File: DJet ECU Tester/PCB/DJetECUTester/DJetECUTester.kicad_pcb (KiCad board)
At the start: 2 copper layers, 93 x 79 mm, 103 parts, among them J1 ISP, J10 ECU3, J2 ECU1, J3 USB_B_Mini, J4 BREAKOUT, J5 12V IN, J6 MPS, J7 VAC, J8 INJECTORS, J9 ECU2, Q1 MMBT2222ALT1G, Q10 MMBT2222ALT1G, Q11 MMBT2222ALT1G, Q12 MMBT3906LT1G, Q13 MMBT3906LT1G, Q14 MMBT3906LT1G, Q2 MMBT2222ALT1G, Q3 MMBT2222ALT1G, Q4 MMBT2222ALT1G, Q5 MMBT2222ALT1G, Q6 MMBT2222ALT1G, Q7 MMBT2222ALT1G, Q8 MMBT2222ALT1G, Q9 MMBT2222ALT1G, U1 ATmega328P, U2 LM2596S-5, U3 FT232RL, U4 MCP41HV51-502E-ST, U5 MCP41HV51-502E-ST, Y1 FA-238 16.0000MB-C3

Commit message: Work in progress.
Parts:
- removed J7: VAC, TerminalBlock_TE-Connectivity:TerminalBlock_TE_282834-6_1x06_P2.54mm_Horizontal
- removed J8: INJECTORS, Britishideas:PhoenixContact_COMBICON_PT_5
- removed JP4: VAC VCC, Connector_PinHeader_2.54mm:PinHeader_1x03_P2.54mm_Vertical
- removed Q13, Q14: MMBT3906LT1G, Package_TO_SOT_SMD:SOT-23
- added C18: 100nF, Capacitor_SMD:C_0805_2012Metric, F.Cu at (299.5, 127.2)
- added C19: 100nF, Capacitor_SMD:C_0805_2012Metric, F.Cu at (464.8, 14.4)
- added C20: 100nF, Capacitor_SMD:C_0805_2012Metric, F.Cu at (463.2, 21.0)
- added D10: MBR0520LT1G, Britishideas:SOD-123, F.Cu at (305.0, 116.4)
- added D5: MBR0520LT1G, Britishideas:SOD-123, F.Cu at (352.3, 92.6)
- added D6: MBR0520LT1G, Britishideas:SOD-123, F.Cu at (357.5, 92.6)
- added D7: MBR0520LT1G, Britishideas:SOD-123, F.Cu at (341.8, 92.6)
- added D8: RED, LED_SMD:LED_PLCC-2, F.Cu at (294.2, 128.1)
- added D9: MBR0520LT1G, Britishideas:SOD-123, F.Cu at (305.0, 113.9)
- added JP1: COOLANTTEMP, Connector_PinHeader_2.54mm:PinHeader_2x01_P2.54mm_Vertical, F.Cu at (456.1, 21.8)
- added L2: 1.5mH, Britishideas:D-Jetronic-Injector-Inductor-Multi-Component, F.Cu at (404.4, 71.8)
- added L3: 1.5mH, Britishideas:D-Jetronic-Injector-Inductor-Multi-Component, F.Cu at (404.4, 32.5)
- added L4: 1.5mH, Britishideas:D-Jetronic-Injector-Inductor-Multi-Component, F.Cu at (365.2, 71.8)
- added L5: 1.5mH, Britishideas:D-Jetronic-Injector-Inductor-Multi-Component, F.Cu at (365.2, 32.5)
- added L6: 1.5mH, Britishideas:D-Jetronic-Injector-Inductor-Multi-Component, F.Cu at (286.7, 32.5)
- added L7: 1.5mH, Britishideas:D-Jetronic-Injector-Inductor-Multi-Component, F.Cu at (326.0, 71.8)
- added L8: 1.5mH, Britishideas:D-Jetronic-Injector-Inductor-Multi-Component, F.Cu at (326.0, 32.5)
- added L9: 1.5mH, Britishideas:D-Jetronic-Injector-Inductor-Multi-Component, F.Cu at (286.7, 71.8)
- added R39: 11k, Resistor_SMD:R_0805_2012Metric, F.Cu at (368.3, 92.8)
- added R40: 10k, Resistor_SMD:R_0805_2012Metric, F.Cu at (343.0, 99.9)
- added R41: 11k, Resistor_SMD:R_0805_2012Metric, F.Cu at (446.7, 14.4)
- added R42: 10k, Resistor_SMD:R_0805_2012Metric, F.Cu at (442.3, 17.4)
- added R43: 11k, Resistor_SMD:R_0805_2012Metric, F.Cu at (351.9, 105.8)
- added R44: 1K, Resistor_SMD:R_0805_2012Metric, F.Cu at (308.3, 128.0)
- added R45: 100k, Resistor_SMD:R_0805_2012Metric, F.Cu at (469.2, 14.4)
- added R46: 2.7, Britishideas:Chip Resistor 5329 13573 Metric, F.Cu at (312.1, 104.0)
- added R47: 2.7, Britishideas:Chip Resistor 5329 13573 Metric, F.Cu at (327.6, 95.6)
- added R48: 4k2, Resistor_SMD:R_0805_2012Metric, F.Cu at (308.3, 125.1)
- added R49: 4k2, Resistor_SMD:R_0805_2012Metric, F.Cu at (303.9, 127.2)
- added R50: 2.7, Britishideas:Chip Resistor 5329 13573 Metric, F.Cu at (312.1, 95.6)
- added R51: 2.7, Britishideas:Chip Resistor 5329 13573 Metric, F.Cu at (327.6, 104.0)
- added R52: 10k, Resistor_SMD:R_0805_2012Metric, F.Cu at (306.2, 122.1)
- added R53: 10k, Resistor_SMD:R_0805_2012Metric, F.Cu at (306.2, 119.2)
- added R54: 2.7, Britishideas:Chip Resistor 5329 13573 Metric, F.Cu at (296.6, 104.0)
- added R55: 2.7, Britishideas:Chip Resistor 5329 13573 Metric, F.Cu at (281.1, 104.0)
- added R58: 2.7, Britishideas:Chip Resistor 5329 13573 Metric, F.Cu at (296.6, 95.6)
- added R59: 2.7, Britishideas:Chip Resistor 5329 13573 Metric, F.Cu at (281.1, 95.6)
- added TP10: TestPoint, TestPoint:TestPoint_Pad_D2.0mm, F.Cu at (467.4, 22.0)
- added TP11: TestPoint, TestPoint:TestPoint_Pad_D2.0mm, F.Cu at (469.0, 17.9)
- added U6: MCP23S08T-E_SO, Package_SO:SOIC-18W_7.5x11.6mm_P1.27mm, F.Cu at (297.5, 119.2)
- added U7: MCP41HV51-502E-ST, Package_SO:TSSOP-14_4.4x5mm_P0.65mm, F.Cu at (458.1, 16.2)
- D1: value RED -> MBR0520LT1G; footprint LED_SMD:LED_PLCC-2 -> Britishideas:SOD-123
- J4: value BREAKOUT -> 12V 4A IN (5.5/2.5); footprint Connector_PinHeader_2.54mm:PinHeader_2x13_P2.54mm_Vertical -> Connector_BarrelJack:BarrelJack_Wuerth_6941xx301002
- Q12: value MMBT3906LT1G -> MMBT2222ALT1G
- R25, R26, R32, R33, R38: value 1k -> 10k
- R28, R29, R30: value 10k -> 100k
- R31: value 1k -> 100k
- R37: value 10k -> 11k
- R5: value 1K -> 10k
- moved R36 273.3 mm to (437.9, 14.4), turned to 0 degrees
- moved R25 260.8 mm to (437.9, 20.3)
- moved R34 240.5 mm to (442.3, 14.4), turned to 0 degrees
- moved R38 228.1 mm to (437.9, 17.4), turned to 0 degrees
- moved R31 165.3 mm to (351.9, 99.9), turned to 0 degrees
- moved R28 163.6 mm to (356.3, 102.9), turned to 0 degrees
- moved R5 160.7 mm to (360.7, 99.9), turned to 0 degrees
- moved R26 160.3 mm to (356.3, 99.9)
- moved R27 159.4 mm to (351.9, 102.9), turned to 0 degrees
- moved R29 158.0 mm to (347.4, 105.8), turned to 0 degrees
- moved Q10 153.2 mm to (347.5, 96.2), turned to 0 degrees
- moved R37 152.3 mm to (343.0, 105.8), turned to 0 degrees
- moved Q9 152.2 mm to (343.1, 96.2), turned to 0 degrees
- moved R30 150.8 mm to (347.4, 99.9), turned to 0 degrees
- moved R32 149.9 mm to (343.0, 102.9)
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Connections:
- net /~COOLANTTEMP_CS renamed /~COOLANTTEMP1_CS
- D1 pad 2: +5V -> Net-(D1-Pad2)
- J10 pad 7: /ECU_DIAGGROUP13-25 -> (no net)
- J4 pad 1: /ECU_AIRTEMP-1 -> +12V
- J4 pad 2: /ECU_TPSWOT-2 -> GND
- J4 pad 3: /ECU_INJGROUP1-3 -> GND
- Q10 pad 1: Net-(Q10-Pad1) -> Net-(D5-Pad1)
- Q10 pad 3: Net-(J7-Pad4) -> Net-(Q10-Pad3)
- Q11 pad 1: Net-(Q11-Pad1) -> Net-(D6-Pad1)
- Q12 pad 1: Net-(Q12-Pad1) -> Net-(D7-Pad1)
- Q12 pad 2: +12V -> GND
- Q12 pad 3: /ECU_START-18 -> Net-(Q12-Pad3)
- Q9 pad 1: Net-(Q9-Pad1) -> Net-(D1-Pad1)
- Q9 pad 3: Net-(J7-Pad2) -> Net-(Q9-Pad3)
- R25 pad 1: Net-(Q9-Pad1) -> Net-(D5-Pad2)
- R25 pad 2: /VAC1 -> /ECU_INJGROUP2-4
- R26 pad 1: Net-(Q10-Pad1) -> Net-(D6-Pad2)
- R26 pad 2: /VAC2 -> /ECU_INJGROUP4-6
- R27 pad 1: Net-(Q9-Pad1) -> Net-(D7-Pad2)
- R27 pad 2: GND -> /ECU_INJGROUP3-5
- R28 pad 1: Net-(Q10-Pad1) -> Net-(D1-Pad1)
- R29 pad 1: /Vacuum/VACVCC -> Net-(D5-Pad1)
- R29 pad 2: Net-(J7-Pad2) -> GND
- R30 pad 1: /Vacuum/VACVCC -> Net-(D6-Pad1)
- R30 pad 2: Net-(J7-Pad4) -> GND
- R31 pad 1: Net-(Q13-Pad1) -> Net-(D7-Pad1)
- R31 pad 2: Net-(J7-Pad2) -> GND
- R32 pad 1: Net-(Q14-Pad1) -> +12V
- R32 pad 2: Net-(J7-Pad4) -> Net-(Q9-Pad3)
- R33 pad 1: Net-(Q11-Pad1) -> +12V
- R33 pad 2: /START -> Net-(Q10-Pad3)
- R34 pad 1: Net-(Q11-Pad1) -> +12V
- R34 pad 2: GND -> Net-(Q11-Pad3)
- R35 pad 2: Net-(Q11-Pad3) -> Net-(Q12-Pad3)
- R36 pad 1: Net-(J7-Pad3) -> Net-(Q9-Pad3)
- R36 pad 2: GND -> /MCU_INJGROUP1-3
- R37 pad 1: Net-(J7-Pad5) -> /MCU_INJGROUP1-3
- R38 pad 1: Net-(Q12-Pad1) -> Net-(Q10-Pad3)
- R38 pad 2: Net-(Q11-Pad3) -> /MCU_INJGROUP2-4
- R5 pad 1: Net-(D1-Pad1) -> Net-(D1-Pad2)
- R5 pad 2: /STATUS -> /ECU_INJGROUP1-3
- TP4 pad 1: GND -> Net-(JP1-Pad1)
- U1 pad 11: /START -> /MCU_INJGROUP2-4
- U1 pad 12: /TPSWOT -> /~COOLANTTEMP2_CS
- U1 pad 19: Net-(U1-Pad19) -> (no net)
- U1 pad 2: /VAC1 -> /MCU_INJGROUP3-5
- U1 pad 22: Net-(U1-Pad22) -> (no net)
- U1 pad 23: /TPSIDLE -> /MCU_INJGROUP4-6
- U1 pad 24: /TPSACCEL2 -> (no net)
- U1 pad 25: /TPSACCEL1 -> /~IO_CS
- U1 pad 32: /VAC2 -> /MCU_INJGROUP1-3
- U3 pad 10: Net-(U3-Pad10) -> (no net)
- U3 pad 11: Net-(U3-Pad11) -> (no net)
- U3 pad 12: Net-(U3-Pad12) -> (no net)
- U3 pad 13: Net-(U3-Pad13) -> (no net)
- U3 pad 14: Net-(U3-Pad14) -> (no net)
- U3 pad 19: Net-(U3-Pad19) -> (no net)
- U3 pad 22: Net-(U3-Pad22) -> (no net)
- U3 pad 23: Net-(U3-Pad23) -> (no net)
- U3 pad 27: Net-(U3-Pad27) -> (no net)
- U3 pad 28: Net-(U3-Pad28) -> (no net)
- U3 pad 3: Net-(U3-Pad3) -> (no net)
- U3 pad 6: Net-(U3-Pad6) -> (no net)
- U3 pad 9: Net-(U3-Pad9) -> (no net)
- U4 pad 13: Net-(U4-Pad13) -> (no net)
- U4 pad 8: Net-(U4-Pad8) -> (no net)
- U5 pad 11: GND -> Net-(JP1-Pad1)
- U5 pad 13: Net-(U5-Pad13) -> (no net)
- U5 pad 8: Net-(U5-Pad8) -> (no net)
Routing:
- net /MPS-15: track 146.9 -> 0.00 mm, vias 5 -> 0
- net /ECU_TPSIDLE-17: track 111.3 -> 0.00 mm, vias 1 -> 0
- net +12V: track 177.9 -> 70.9 mm, vias 7 -> 2
- net /MPS-7: track 103.5 -> 0.00 mm, vias 2 -> 0
- net /ECU_AIRTEMP-1: track 102.1 -> 0.00 mm, vias 2 -> 0
- net /ECU_TPSACCEL1-9: track 101.0 -> 0.00 mm, vias 1 -> 0
- net /ECU_TPSWOT-2: track 97.1 -> 0.13 mm, vias 2 -> 0
- net /ECU_START-18: track 79.7 -> 0.00 mm, vias 5 -> 0
- net /MPS-10: track 103.0 -> 29.5 mm, vias 3 -> 2
- net /ECU_INJGROUP1-3: track 74.7 -> 9.94 mm, vias 2 -> 0
- net /ECU_TPSACCEL2-20: track 61.4 -> 0.00 mm, vias 2 -> 0
- net /ECU_INJGROUP2-4: track 66.3 -> 10.0 mm, vias 3 -> 1
- net /Vacuum/VACVCC: track 47.5 -> 0.00 mm, vias 2 -> 0
- net /ECU_FUELPUMPRELAY-19: track 46.2 -> 0.00 mm, vias 2 -> 0
- net /START: track 43.6 -> 0.00 mm, vias 2 -> 0
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- removed copper zone on B.Cu, net GND
- removed copper zone on F.Cu, net GND
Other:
- board text added: "(C) ANDY@BRITISHIDEAS.COM 2022"
- board text added: "MERCEDES V8 DJET ECU TESTER V2.0"
- board text removed: "(C) ANDY@BRITISHIDEAS.COM 2021"
- board text removed: "5V"
- board text removed: "BRKOUT"
- board text removed: "G"
- board text removed: "INJ GRP"
- board text removed: "MERCEDES V8 DJET ECU TESTER V1.1"
- board text removed: "VAC"
- board text removed: "VACVCC"
- board text removed: "VCC"
- board text removed: "X"

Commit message: Working on new PCB.
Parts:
- removed R55, R58, R59: 2.7, Britishideas:Chip Resistor 5329 13573 Metric
- added D11: RED, LED_SMD:LED_PLCC-2, F.Cu at (328.1, 73.5)
- added J7: Conn_01x01, Britishideas:tabconnector-63849-1, F.Cu at (317.5, 78.5)
- added J8: Conn_01x01, Britishideas:tabconnector-63849-1, F.Cu at (322.5, 78.5)
- added L10: 680uH, Britishideas:Inductor-MSS1210-684KED, F.Cu at (310.5, 129.5)
- added L11: 680uH, Britishideas:Inductor-MSS1210-684KED, F.Cu at (296.5, 129.5)
- added L12: 680uH, Britishideas:Inductor-MSS1210-684KED, F.Cu at (282.0, 129.5)
- added L13: 680uH, Britishideas:Inductor-MSS1210-684KED, F.Cu at (268.0, 129.5)
- added L14: 680uH, Britishideas:Inductor-MSS1210-684KED, F.Cu at (310.5, 116.0)
- added L15: 680uH, Britishideas:Inductor-MSS1210-684KED, F.Cu at (296.5, 116.0)
- added L16: 680uH, Britishideas:Inductor-MSS1210-684KED, F.Cu at (282.0, 116.0)
- added L17: 680uH, Britishideas:Inductor-MSS1210-684KED, F.Cu at (268.0, 116.0)
- L2, L3, L4, L5, L6, L7, L8, L9: value 1.5mH -> 680uH; footprint Britishideas:D-Jetronic-Injector-Inductor-Multi-Component -> Britishideas:Inductor-MSS1210-684KED
- R46, R47, R50, R51: value 2.7 -> 50; footprint Britishideas:Chip Resistor 5329 13573 Metric -> Britishideas:Potentometer_Bourns_PV36W
- R54: value 2.7 -> 2k6; footprint Britishideas:Chip Resistor 5329 13573 Metric -> Resistor_SMD:R_0805_2012Metric
- moved R45 268.6 mm to (211.4, 89.7)
- moved C19 264.1 mm to (210.8, 87.0), turned to 90 degrees
- moved C20 256.1 mm to (213.8, 79.5)
- moved U7 252.8 mm to (214.8, 84.8), turned to 90 degrees
- moved TP10 251.7 mm to (221.8, 76.6)
- moved TP11 250.5 mm to (225.5, 76.6)
- moved JP1 242.0 mm to (221.8, 82.4), turned to 90 degrees
- moved L3 121.8 mm to (296.5, 89.0), turned to 270 degrees
- moved L5 112.4 mm to (268.0, 89.0), turned to 270 degrees
- moved R44 104.3 mm to (205.7, 109.4), turned to 90 degrees
- moved L2 95.5 mm to (310.5, 89.0), turned to 270 degrees
- moved D8 94.7 mm to (201.4, 109.7), turned to 180 degrees
- moved R25 89.0 mm to (363.9, 69.8)
- moved R34 89.0 mm to (368.3, 63.9)
- moved R36 89.0 mm to (363.9, 63.9)
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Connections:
- J2 pad 1: +12V -> /ECU_PWR
- J2 pad 2: +12V -> /ECU_PWR
- L2 pad 1: Net-(L2-Pad1) -> /ECU_INJGROUP1-3
- L2 pad 2: /ECU_INJGROUP1-3 -> Net-(L2-Pad2)
- L3 pad 1: Net-(L3-Pad1) -> Net-(L2-Pad2)
- L3 pad 2: /ECU_INJGROUP3-5 -> Net-(L3-Pad2)
- L4 pad 1: Net-(L4-Pad1) -> Net-(L3-Pad2)
- L4 pad 2: /ECU_INJGROUP3-5 -> Net-(L4-Pad2)
- L5 pad 1: Net-(L5-Pad1) -> Net-(L4-Pad2)
- L5 pad 2: /ECU_INJGROUP1-3 -> GND
- L6 pad 1: Net-(L6-Pad1) -> /ECU_INJGROUP2-4
- L6 pad 2: /ECU_INJGROUP4-6 -> Net-(L6-Pad2)
- L7 pad 1: Net-(L7-Pad1) -> Net-(L6-Pad2)
- L7 pad 2: /ECU_INJGROUP2-4 -> Net-(L7-Pad2)
- L8 pad 1: Net-(L8-Pad1) -> Net-(L7-Pad2)
- L8 pad 2: /ECU_INJGROUP4-6 -> Net-(L8-Pad2)
- L9 pad 1: Net-(L9-Pad1) -> Net-(L8-Pad2)
- L9 pad 2: /ECU_INJGROUP2-4 -> GND
- R46 pad 1: Net-(L2-Pad1) -> /ECU_INJGROUP1-3
- R47 pad 1: Net-(L3-Pad1) -> /ECU_INJGROUP2-4
- R50 pad 1: Net-(L4-Pad1) -> /ECU_INJGROUP4-6
- R51 pad 1: Net-(L5-Pad1) -> /ECU_INJGROUP3-5
- R54 pad 1: Net-(L6-Pad1) -> Net-(D11-Pad1)
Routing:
- net +12V: track 70.9 -> 201.4 mm
- net /ECU_INJGROUP1-3: track 9.94 -> 125.1 mm, vias 0 -> 2
- net /ECU_INJGROUP2-4: track 10.0 -> 107.7 mm, vias 1 -> 2
- net /ECU_TPSIDLE-17: track 0.00 -> 91.2 mm, vias 0 -> 3
- net /ECU_INJGROUP3-5: track 11.9 -> 98.3 mm, vias 1 -> 2
- net /ECU_INJGROUP4-6: track 11.9 -> 92.9 mm, vias 1 -> 0
- net /MPS-8: track 79.8 -> 0.00 mm, vias 1 -> 0
- net /ECU_TPSACCEL1-9: track 0.00 -> 73.8 mm, vias 0 -> 3
- net /ECU_TPSACCEL2-20: track 0.00 -> 73.6 mm, vias 0 -> 3
- net /ECU_TPSWOT-2: track 0.13 -> 63.2 mm, vias 0 -> 1
- net /ECU_COOLANTTEMP-23: track 0.00 -> 52.0 mm, vias 0 -> 3
- net /ECU_TRIGGERGROUP1-21: track 0.00 -> 50.5 mm, vias 0 -> 5
- net /ECU_AIRTEMP-1: track 0.00 -> 49.4 mm, vias 0 -> 1
- net /MPS-10: track 29.5 -> 1.27 mm, vias 2 -> 0
- net Net-(JP1-Pad1): track 0.00 -> 25.8 mm, vias 0 -> 3
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- added copper zone on B.Cu, net GND
- added copper zone on F.Cu, net GND
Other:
- board size 93 x 79 mm -> 162 x 90 mm
- board text added: "ECU PWR"

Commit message: Working on new PCB.
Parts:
- moved R35 167.9 mm to (245.2, 132.4), turned to 180 degrees
- moved R39 164.3 mm to (245.2, 117.6)
- moved D6 162.4 mm to (250.6, 139.4)
- moved Q11 158.1 mm to (247.2, 138.6), turned to 180 degrees
- moved Q12 156.6 mm to (247.2, 129.6), turned to 180 degrees
- moved R26 154.3 mm to (252.8, 137.6)
- moved R40 151.1 mm to (244.4, 138.8), turned to 90 degrees
- moved R30 148.9 mm to (250.0, 136.8), turned to 90 degrees
- moved R43 148.1 mm to (245.2, 127.0)
- moved D5 147.7 mm to (250.4, 121.0)
- moved R31 147.6 mm to (249.8, 127.7), turned to 90 degrees
- moved R41 146.4 mm to (245.2, 135.8)
- moved R34 145.5 mm to (245.2, 141.4), turned to 180 degrees
- moved D7 144.8 mm to (250.2, 130.4)
- moved R27 144.1 mm to (252.6, 128.6)
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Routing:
- net /MPS-7: track 0.00 -> 63.3 mm
- net /MPS-8: track 0.00 -> 52.6 mm
- net /MPS-10: track 1.27 -> 38.2 mm
- net /ECU_TRIGGERGROUP2-13: track 63.7 -> 40.2 mm
- net /ECU_TRIGGERGROUP3-22: track 47.1 -> 70.3 mm
- net /ECU_TRIGGERGROUP1-21: track 50.5 -> 73.1 mm
- net /ECU_TRIGGERGROUP4-14: track 65.0 -> 42.5 mm
- net /ECU_TPSACCEL2-20: track 73.6 -> 95.4 mm
- net /ECU_COOLANTTEMP-23: track 52.0 -> 73.7 mm
- net /ECU_TPSIDLE-17: track 91.2 -> 70.7 mm
- net /ECU_AIRTEMP-1: track 49.4 -> 67.7 mm, vias 1 -> 3
- net /MPS-15: track 0.00 -> 17.4 mm
- net /ECU_TPSACCEL1-9: track 73.8 -> 56.8 mm, vias 3 -> 1
- net /ECU_TPSWOT-2: track 63.2 -> 75.4 mm, vias 1 -> 3
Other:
- board text added: "ECU I/O"
- board text added: "PWR+INJ"
- board text removed: "(10)"
- board text removed: "(15)"
- board text removed: "(7)"
- board text removed: "(8)"
- board text removed: "bl"
- board text removed: "gn"
- board text removed: "grey +"
- board text removed: "rt"
- board text removed: "sw"

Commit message: Initial routing completed.
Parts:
- moved Q12 0.20 mm to (247.2, 129.8)
- moved R27 0.20 mm to (252.8, 128.6)
- moved R33 0.20 mm to (245.2, 123.2)
- moved R31 0.20 mm to (250.0, 127.7)
- moved R34 0.20 mm to (245.2, 141.6)
- moved R35 0.20 mm to (245.2, 132.6)
- moved R39 0.20 mm to (245.2, 117.4)
- moved R25 0.11 mm to (252.8, 119.2)
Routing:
- net +12V: track 201.4 -> 275.8 mm, vias 2 -> 7
- net /ECU_START-18: track 0.00 -> 65.5 mm, vias 0 -> 3
- net /MCU_INJGROUP1-3: track 0.00 -> 63.4 mm, vias 0 -> 4
- net /ECU_FUELPUMPRELAY-19: track 0.00 -> 62.5 mm, vias 0 -> 3
- net /MISO: track 41.9 -> 103.7 mm, vias 5 -> 11
- net /MOSI: track 42.3 -> 103.9 mm, vias 6 -> 10
- net /SCK: track 45.4 -> 106.3 mm, vias 6 -> 10
- net /~IO_CS: track 0.00 -> 60.8 mm, vias 0 -> 6
- net /MCU_INJGROUP4-6: track 0.00 -> 60.2 mm, vias 0 -> 2
- net +5V: track 176.5 -> 226.2 mm, vias 10 -> 14
- net /MCU_INJGROUP3-5: track 0.00 -> 45.7 mm, vias 0 -> 2
- net /TPSACCEL1: track 22.4 -> 66.5 mm, vias 2 -> 6
- net /TPSWOT: track 14.8 -> 53.0 mm, vias 0 -> 6
- net /MCU_INJGROUP2-4: track 0.00 -> 36.4 mm, vias 0 -> 2
- net /~COOLANTTEMP2_CS: track 4.06 -> 38.3 mm, vias 0 -> 2
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
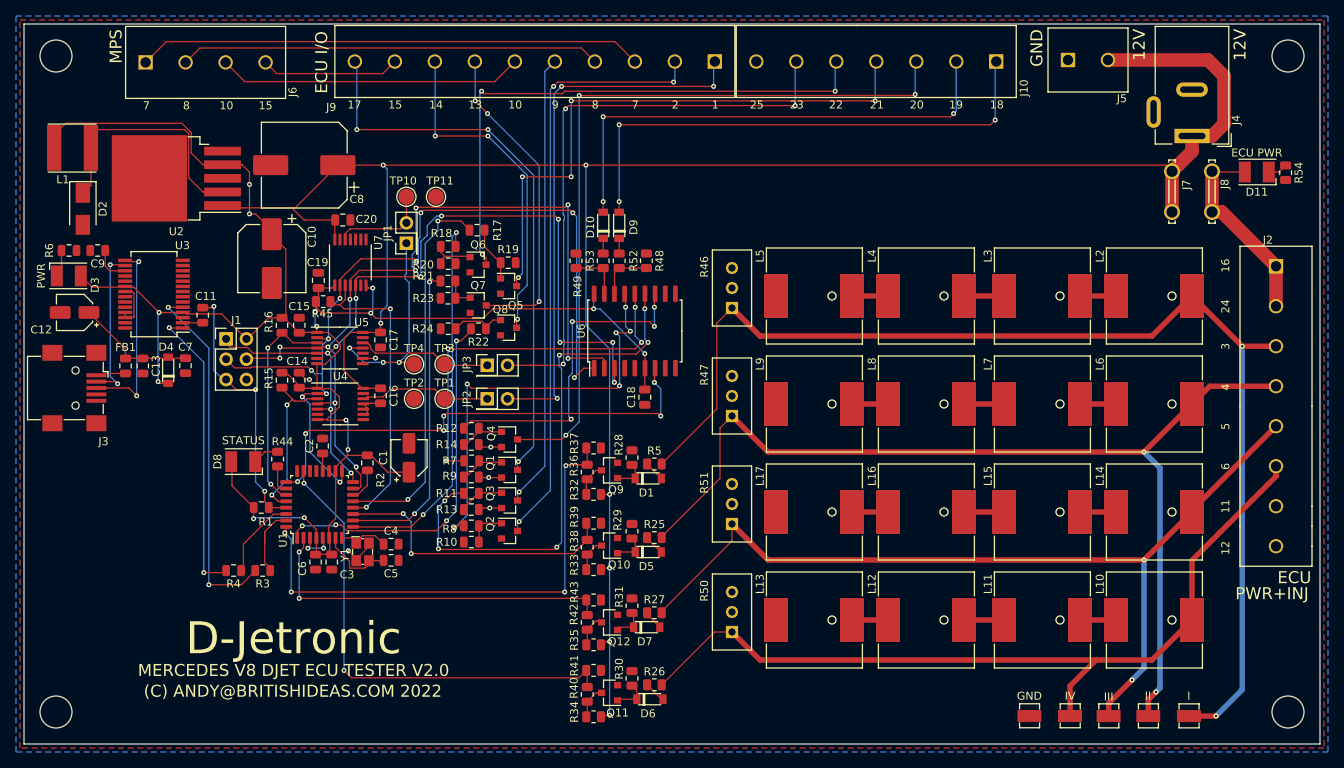
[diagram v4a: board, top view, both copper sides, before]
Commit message: Tweaked PCB layout, added basic ground stitching vias. Regenerated BOM.
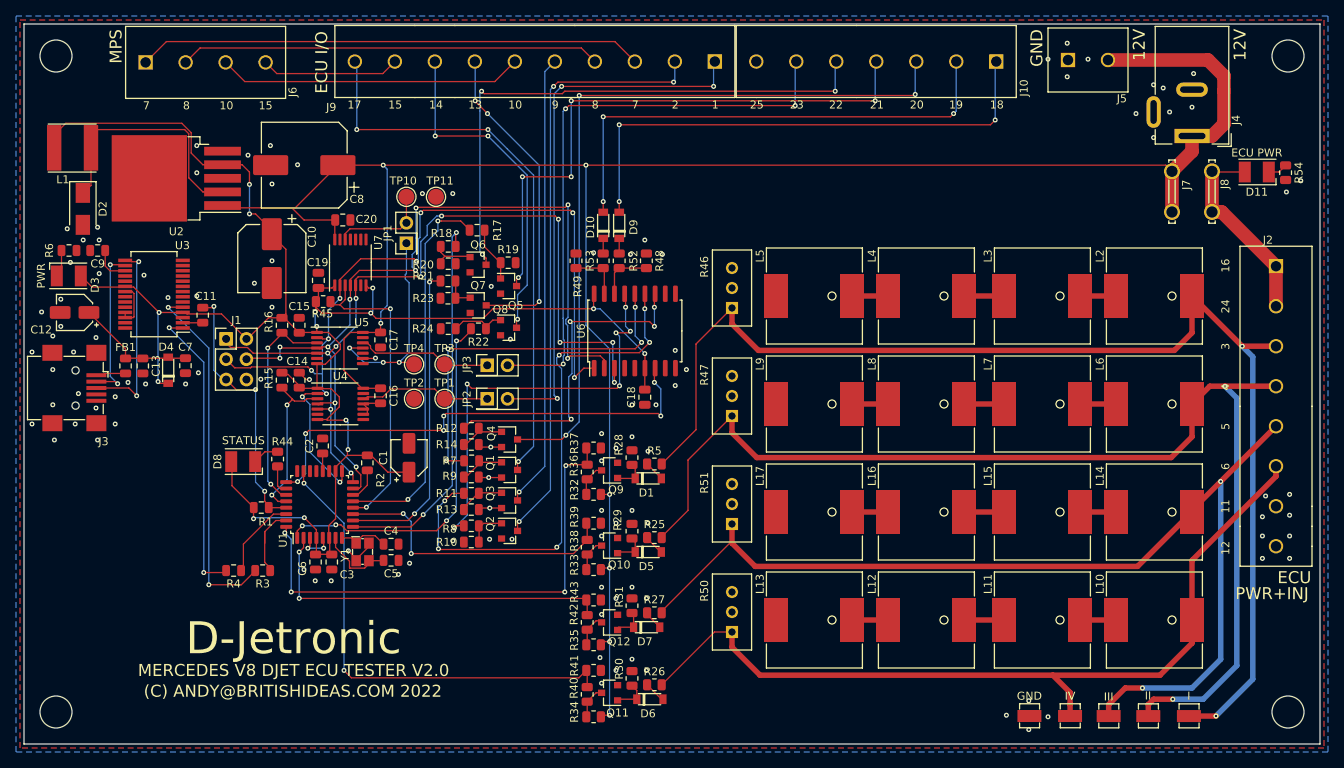
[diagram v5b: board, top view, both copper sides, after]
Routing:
- net /ECU_INJGROUP3-5: track 113.1 -> 133.8 mm
- net /ECU_INJGROUP2-4: track 126.6 -> 146.4 mm
- net /ECU_INJGROUP1-3: track 148.3 -> 154.7 mm
- net /ECU_INJGROUP4-6: track 104.5 -> 106.6 mm
- net /TPSACCEL1: track 66.5 -> 67.0 mm
- net GND: vias 8 -> 114

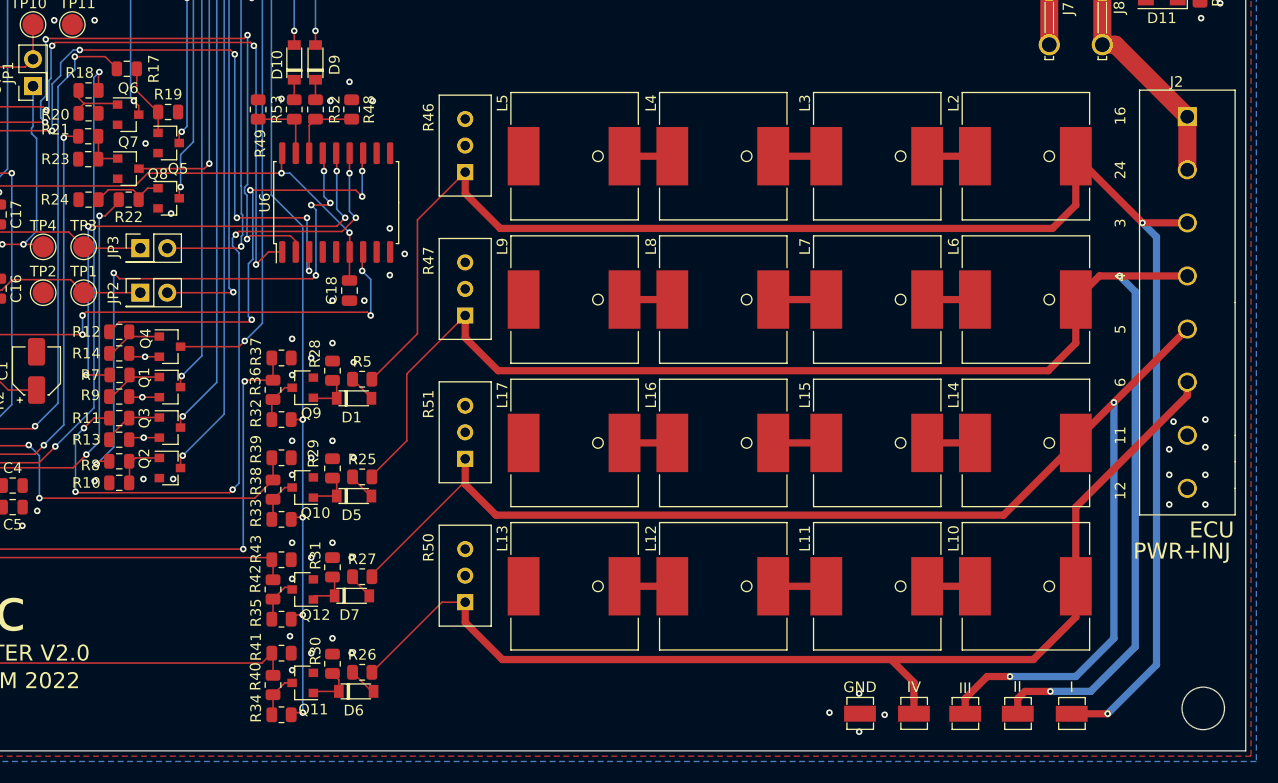
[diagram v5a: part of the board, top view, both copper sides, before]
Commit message: Added test points from trimpots. Added ground stitching vias around inductors.
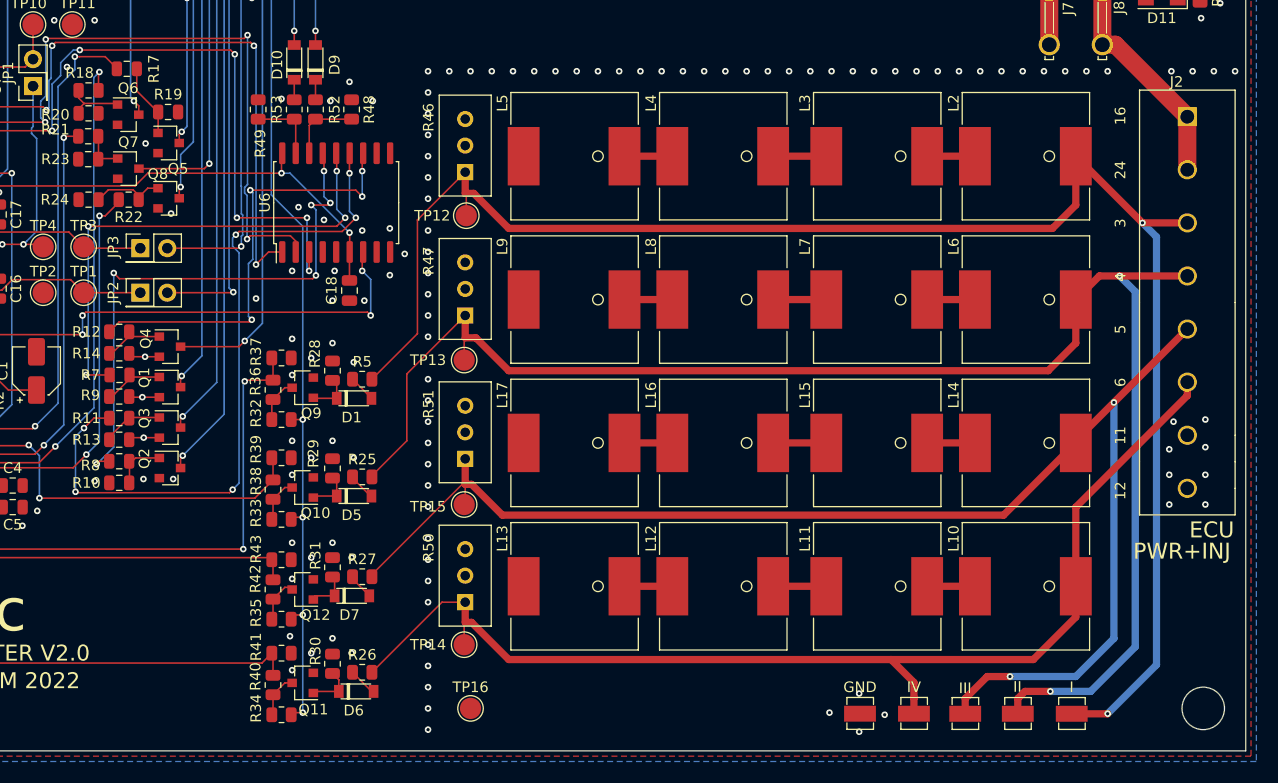
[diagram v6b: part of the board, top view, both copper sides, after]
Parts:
- added TP12: TestPoint, TestPoint:TestPoint_Pad_D2.0mm, F.Cu at (262.6, 94.6)
- added TP13: TestPoint, TestPoint:TestPoint_Pad_D2.0mm, F.Cu at (262.4, 108.2)
- added TP14: TestPoint, TestPoint:TestPoint_Pad_D2.0mm, F.Cu at (262.4, 135.0)
- added TP15: TestPoint, TestPoint:TestPoint_Pad_D2.0mm, F.Cu at (262.4, 121.8)
- added TP16: TestPoint, TestPoint:TestPoint_Pad_D2.0mm, F.Cu at (263.0, 141.0)
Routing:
- net /ECU_INJGROUP4-6: track 106.6 -> 108.7 mm
- net /ECU_INJGROUP2-4: track 146.4 -> 148.6 mm
- net /ECU_INJGROUP1-3: track 154.7 -> 156.9 mm
- net /ECU_INJGROUP3-5: track 133.8 -> 135.8 mm
- net GND: vias 114 -> 186
